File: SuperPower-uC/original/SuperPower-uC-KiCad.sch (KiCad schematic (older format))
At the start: 0 parts

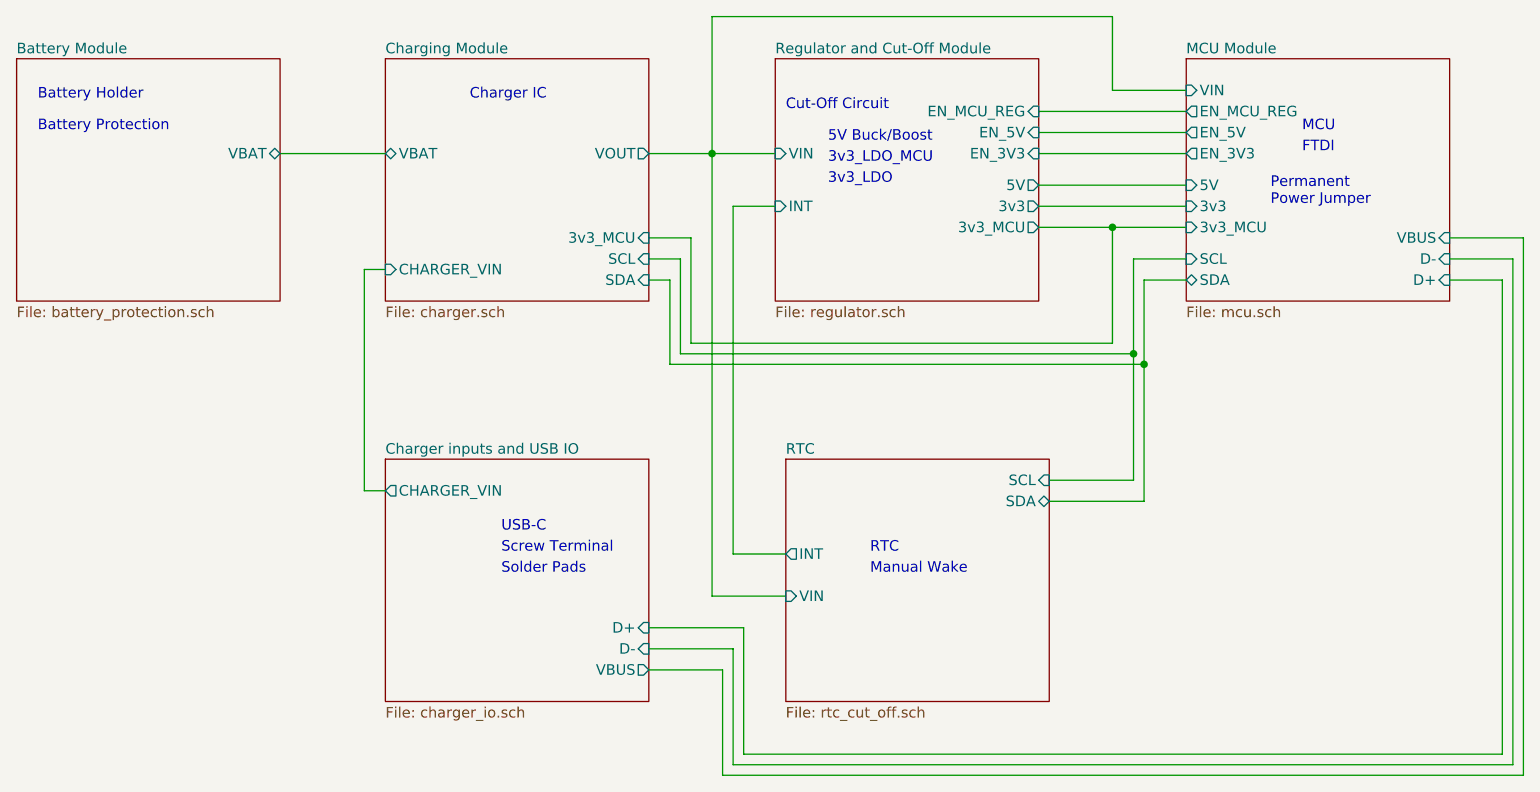
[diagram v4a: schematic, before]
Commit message: Complete rework of regulator design
Removed the old regulator in favor of the TPS63070 and TPS709.
Rewired the RTC and I2C pullups to the TPS709.
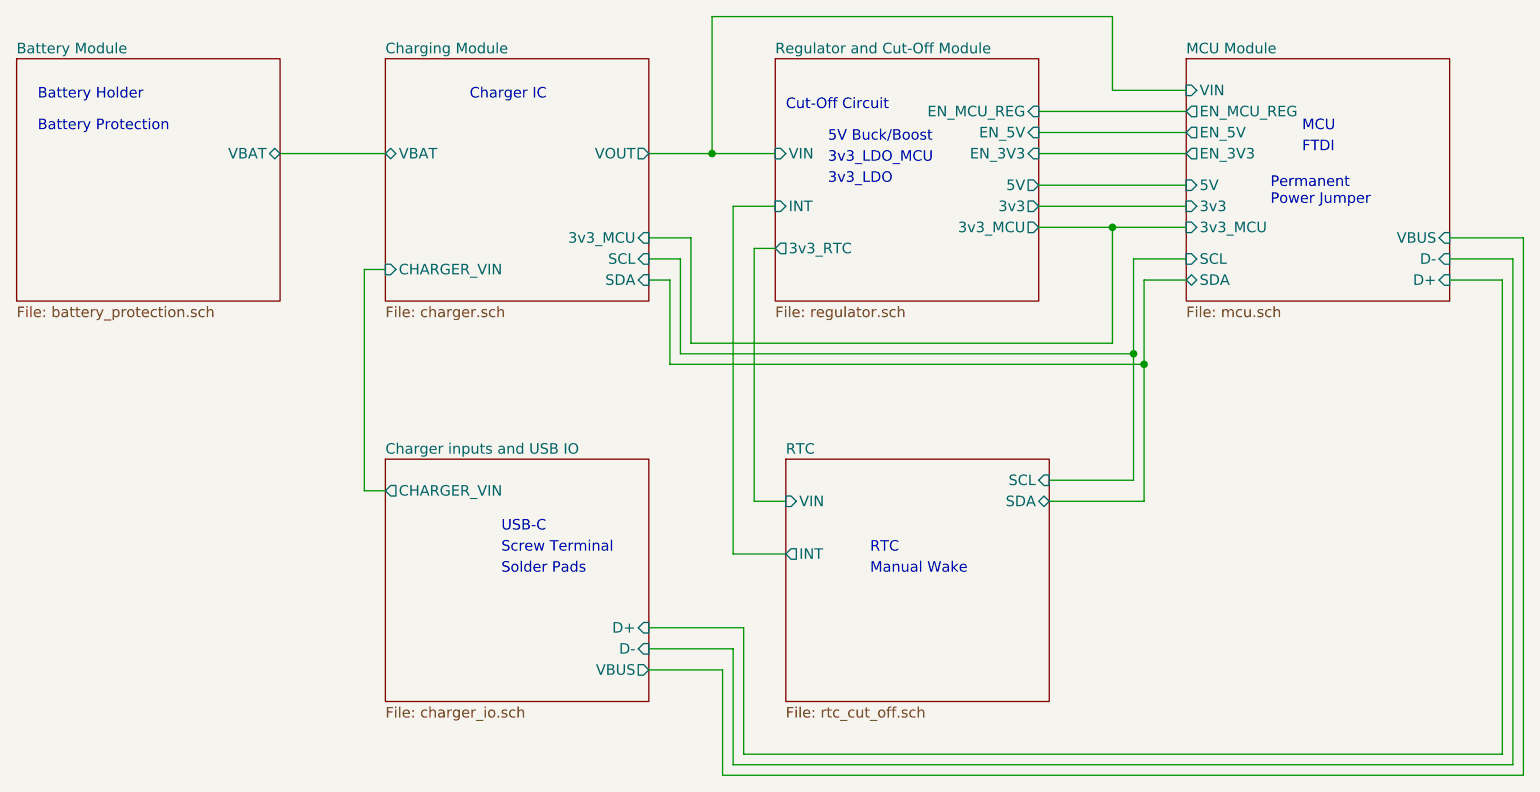
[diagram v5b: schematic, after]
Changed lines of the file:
@@
 F7 "3v3_MCU" I R 4300 2950 50
 $EndSheet
-$Sheet
-S 4950 4000 1250 1150
-U 5F63A00B
-F0 "RTC" 50
-F1 "rtc_cut_off.sch" 50
-F2 "SCL" I R 6200 4100 50
-F3 "SDA" B R 6200 4200 50
-F4 "VIN" I L 4950 4650 50
-F5 "INT" O L 4950 4450 50
-$EndSheet
-$Sheet
-S 6850 2100 1250 1150
-U 5F63A193
-F0 "MCU Module" 50
-F1 "mcu.sch" 50
-F2 "3v3_MCU" I L 6850 2900 50
-F3 "SDA" B L 6850 3150 50
-F4 "SCL" I L 6850 3050 50
-F5 "D+" I R 8100 3150 50
-F6 "D-" I R 8100 3050 50
-F7 "VBUS" I R 8100 2950 50
-F8 "5V" I L 6850 2700 50
-F9 "3v3" I L 6850 2800 50
-F10 "EN_3V3" O L 6850 2550 50
-F11 "EN_5V" O L 6850 2450 50
-F12 "EN_MCU_REG" O L 6850 2350 50
-F13 "VIN" I L 6850 2250 50
-$EndSheet
 Wire Wire Line
 	2550 2550 3050 2550
 Wire Wire Line
-	6850 2900 6500 2900
-Wire Wire Line
 	6850 3150 6650 3150
 Wire Wire Line
@@
 Wire Wire Line
 	4300 2550 4600 2550
-Wire Wire Line
-	4600 2550 4600 4650
-Wire Wire Line
-	4600 4650 4950 4650
 Wire Wire Line
 	4950 4450 4700 4450
@@
 	6850 2550 6150 2550
 Wire Wire Line
+	6150 2700 6850 2700
+Wire Wire Line
+	6150 2450 6850 2450
+$Sheet
+S 3050 4000 1250 1150
+U 5F63B107
+F0 "Charger inputs and USB IO" 50
+F1 "charger_io.sch" 50
+F2 "VBUS" O R 4300 5000 50
+F3 "D+" I R 4300 4800 50
+F4 "D-" I R 4300 4900 50
+F5 "CHARGER_VIN" O L 3050 4150 50
+$EndSheet
+Wire Wire Line
+	3050 3100 2950 3100
+Wire Wire Line
+	2950 3100 2950 4150
+Wire Wire Line
+	2950 4150 3050 4150
+Wire Wire Line
+	4750 4800 4300 4800
+Wire Wire Line
+	4700 4900 4300 4900
+Wire Wire Line
+	8100 2950 8450 2950
+Wire Wire Line
+	8450 2950 8450 5500
+Wire Wire Line
+	8450 5500 4650 5500
+Wire Wire Line
+	4650 5500 4650 5000
+Wire Wire Line
+	4650 5000 4300 5000
+Wire Wire Line
+	6150 2350 6850 2350
+Wire Wire Line
+	4600 2550 4600 1900
+Wire Wire Line
+	4600 1900 6500 1900
+Wire Wire Line
+	6500 1900 6500 2250
+Wire Wire Line
+	6500 2250 6850 2250
+Wire Wire Line
+	4300 2950 4500 2950
+Wire Wire Line
+	4500 2950 4500 3450
+Wire Wire Line
+	4500 3450 6500 3450
+$Sheet
+S 6850 2100 1250 1150
+U 5F63A193
+F0 "MCU Module" 50
+F1 "mcu.sch" 50
+F2 "3v3_MCU" I L 6850 2900 50
+F3 "SDA" B L 6850 3150 50
+F4 "SCL" I L 6850 3050 50
+F5 "D+" I R 8100 3150 50
+F6 "D-" I R 8100 3050 50
+F7 "VBUS" I R 8100 2950 50
+F8 "5V" I L 6850 2700 50
+F9 "3v3" I L 6850 2800 50
+F10 "EN_3V3" O L 6850 2550 50
+F11 "EN_5V" O L 6850 2450 50
+F12 "EN_MCU_REG" O L 6850 2350 50
+F13 "VIN" I L 6850 2250 50
+$EndSheet
+Wire Wire Line
+	6500 3450 6500 2900
+Wire Wire Line
+	6850 2900 6500 2900
+Wire Wire Line
 	6850 2800 6150 2800
+$Sheet
+S 4950 4000 1250 1150
+U 5F63A00B
+F0 "RTC" 50
+F1 "rtc_cut_off.sch" 50
+F2 "SCL" I R 6200 4100 50
+F3 "SDA" B R 6200 4200 50
+F4 "VIN" I L 4950 4200 50
+F5 "INT" O L 4950 4450 50
+$EndSheet
+Wire Wire Line
+	4900 3000 4800 3000
+Wire Wire Line
+	4800 3000 4800 4200
+Wire Wire Line
+	4800 4200 4950 4200
+Connection ~ 6500 2900
+Wire Wire Line
+	6500 2900 6150 2900
 $Sheet
 S 4900 2100 1250 1150
@@
 F8 "EN_5V" I R 6150 2450 50
 F9 "EN_MCU_REG" I R 6150 2350 50
-$EndSheet
-Wire Wire Line
-	6150 2700 6850 2700
-Wire Wire Line
-	6150 2450 6850 2450
-$Sheet
-S 3050 4000 1250 1150
-U 5F63B107
-F0 "Charger inputs and USB IO" 50
-F1 "charger_io.sch" 50
-F2 "VBUS" O R 4300 5000 50
-F3 "D+" I R 4300 4800 50
-F4 "D-" I R 4300 4900 50
-F5 "CHARGER_VIN" O L 3050 4150 50
-$EndSheet
-Wire Wire Line
-	3050 3100 2950 3100
-Wire Wire Line
-	2950 3100 2950 4150
-Wire Wire Line
-	2950 4150 3050 4150
-Wire Wire Line
-	4750 4800 4300 4800
-Wire Wire Line
-	4700 4900 4300 4900
-Wire Wire Line
-	8100 2950 8450 2950
-Wire Wire Line
-	8450 2950 8450 5500
-Wire Wire Line
-	8450 5500 4650 5500
-Wire Wire Line
-	4650 5500 4650 5000
-Wire Wire Line
-	4650 5000 4300 5000
-Wire Wire Line
-	6150 2350 6850 2350
-Wire Wire Line
-	4600 2550 4600 1900
-Wire Wire Line
-	4600 1900 6500 1900
-Wire Wire Line
-	6500 1900 6500 2250
-Wire Wire Line
-	6500 2250 6850 2250
-Wire Wire Line
-	4300 2950 4500 2950
-Wire Wire Line
-	4500 2950 4500 3450
-Wire Wire Line
-	4500 3450 6500 3450
-Wire Wire Line
-	6500 3450 6500 2900
-Connection ~ 6500 2900
-Wire Wire Line
-	6500 2900 6150 2900
+F10 "3v3_RTC" O L 4900 3000 50
+$EndSheet
 $EndSCHEMATC

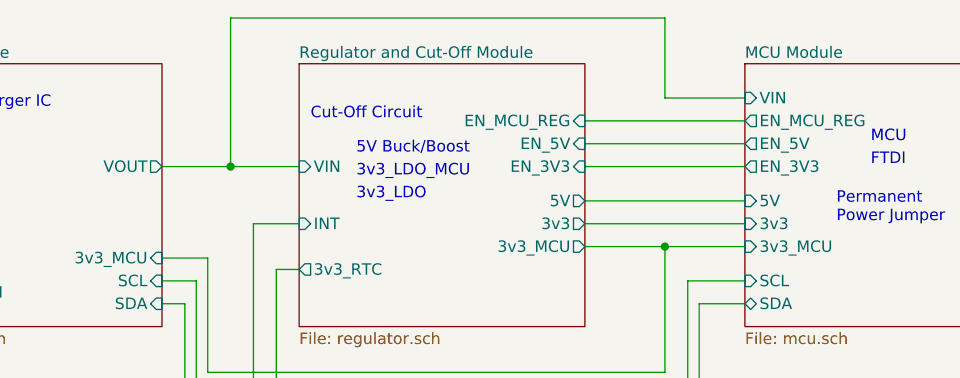
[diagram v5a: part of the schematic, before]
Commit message: Apply first batch of changes fro review ticket
https://github.com/Informaticore/SuperPower/issues/58
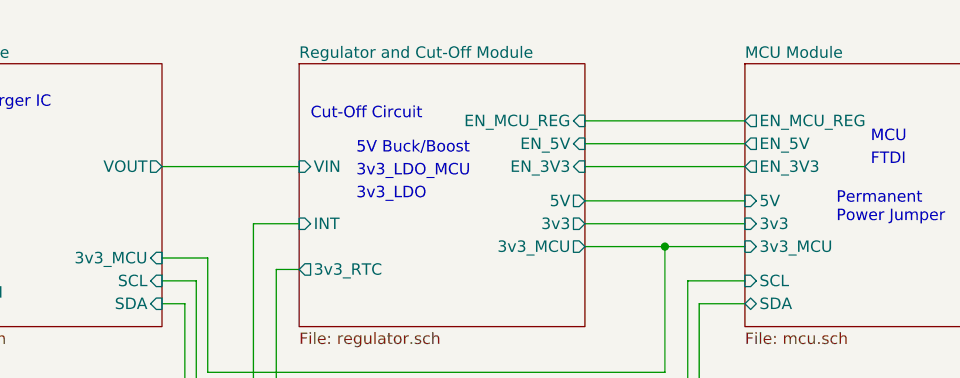
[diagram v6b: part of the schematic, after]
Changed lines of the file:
@@
 	6600 4100 6200 4100
-Wire Wire Line
-	4300 2550 4600 2550
 Wire Wire Line
 	4950 4450 4700 4450
@@
 FTDI
 Wire Wire Line
-	4600 2550 4900 2550
-Connection ~ 4600 2550
-Wire Wire Line
 	6850 2550 6150 2550
 Wire Wire Line
@@
 	6150 2350 6850 2350
 Wire Wire Line
-	4600 2550 4600 1900
-Wire Wire Line
-	4600 1900 6500 1900
-Wire Wire Line
-	6500 1900 6500 2250
-Wire Wire Line
-	6500 2250 6850 2250
-Wire Wire Line
 	4300 2950 4500 2950
 Wire Wire Line
@@
 F11 "EN_5V" O L 6850 2450 50
 F12 "EN_MCU_REG" O L 6850 2350 50
-F13 "VIN" I L 6850 2250 50
 $EndSheet
 Wire Wire Line
@@
 F10 "3v3_RTC" O L 4900 3000 50
 $EndSheet
+Wire Wire Line
+	4300 2550 4900 2550
 $EndSCHEMATC

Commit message: Applied more changes from review
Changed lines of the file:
@@
 F2 "SCL" I R 6200 4100 50
 F3 "SDA" B R 6200 4200 50
-F4 "VIN" I L 4950 4200 50
+F4 "3v3_RTC" I L 4950 4200 50
 F5 "INT" O L 4950 4450 50
 $EndSheet

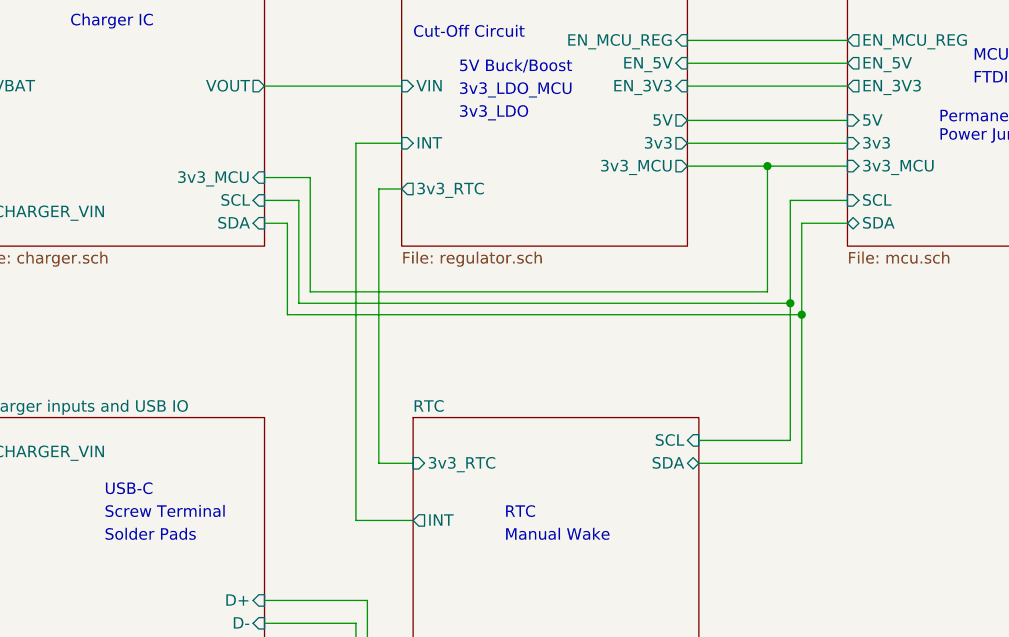
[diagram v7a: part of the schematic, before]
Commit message: Update Global Labels on main sheet and sub-sheets
3V3_RTC updates
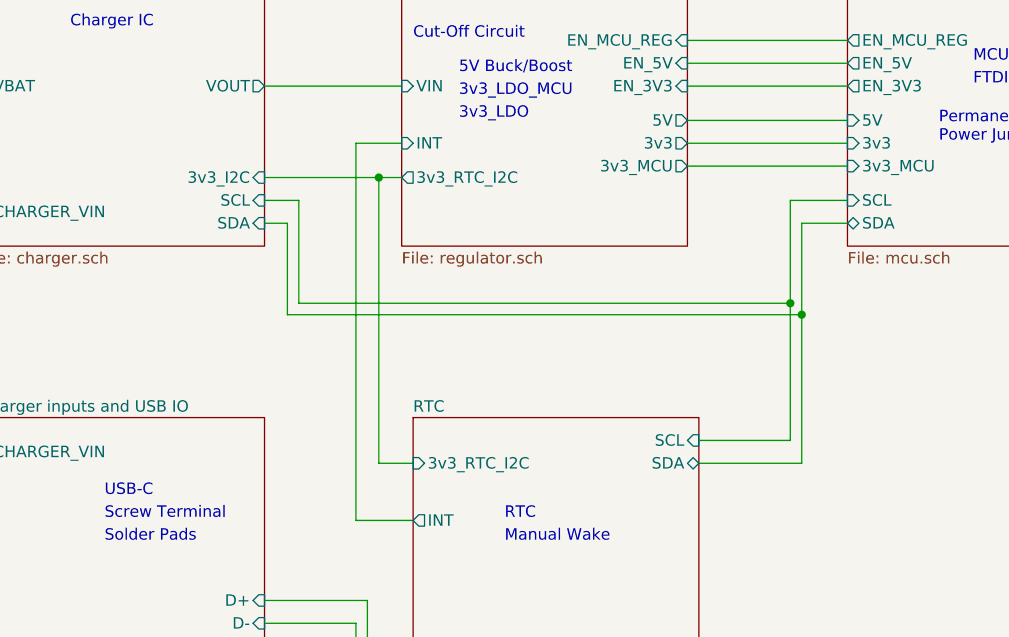
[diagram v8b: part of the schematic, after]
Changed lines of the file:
@@
 F5 "SCL" I R 4300 3050 50
 F6 "SDA" I R 4300 3150 50
-F7 "3v3_MCU" I R 4300 2950 50
+F7 "3v3_I2C" I R 4300 2950 50
 $EndSheet
 Wire Wire Line
@@
 Wire Wire Line
 	6150 2350 6850 2350
-Wire Wire Line
-	4300 2950 4500 2950
-Wire Wire Line
-	4500 2950 4500 3450
-Wire Wire Line
-	4500 3450 6500 3450
 $Sheet
 S 6850 2100 1250 1150
@@
 $EndSheet
 Wire Wire Line
-	6500 3450 6500 2900
-Wire Wire Line
-	6850 2900 6500 2900
-Wire Wire Line
 	6850 2800 6150 2800
 $Sheet
@@
 F2 "SCL" I R 6200 4100 50
 F3 "SDA" B R 6200 4200 50
-F4 "3v3_RTC" I L 4950 4200 50
+F4 "3v3_RTC_I2C" I L 4950 4200 50
 F5 "INT" O L 4950 4450 50
 $EndSheet
 Wire Wire Line
-	4900 3000 4800 3000
-Wire Wire Line
-	4800 3000 4800 4200
-Wire Wire Line
 	4800 4200 4950 4200
-Connection ~ 6500 2900
-Wire Wire Line
-	6500 2900 6150 2900
 $Sheet
 S 4900 2100 1250 1150
@@
 F8 "EN_5V" I R 6150 2450 50
 F9 "EN_MCU_REG" I R 6150 2350 50
-F10 "3v3_RTC" O L 4900 3000 50
+F10 "3v3_RTC_I2C" O L 4900 2950 50
 $EndSheet
 Wire Wire Line
 	4300 2550 4900 2550
+Wire Wire Line
+	6150 2900 6850 2900
+Wire Wire Line
+	4300 2950 4800 2950
+Wire Wire Line
+	4800 2950 4800 4200
+Wire Wire Line
+	4800 2950 4900 2950
+Connection ~ 4800 2950
 $EndSCHEMATC
